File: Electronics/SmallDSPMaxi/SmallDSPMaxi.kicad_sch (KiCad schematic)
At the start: 94 parts, among them J1 Header, J10 Header, J11 Programming, J2 Header, J3 Header, J4 Header, J5 Header, J6 Header, J7 Header, J8 Header, J9 Header, Q1 NSS1C300ET4G, SW1 SW_4PDT, SW2 TS-1187A-B-A-B, SW3 CJS-1201TB, U1 ADAU1467, U2 ADM811, U3 M95M01-R, Y1 830105957509

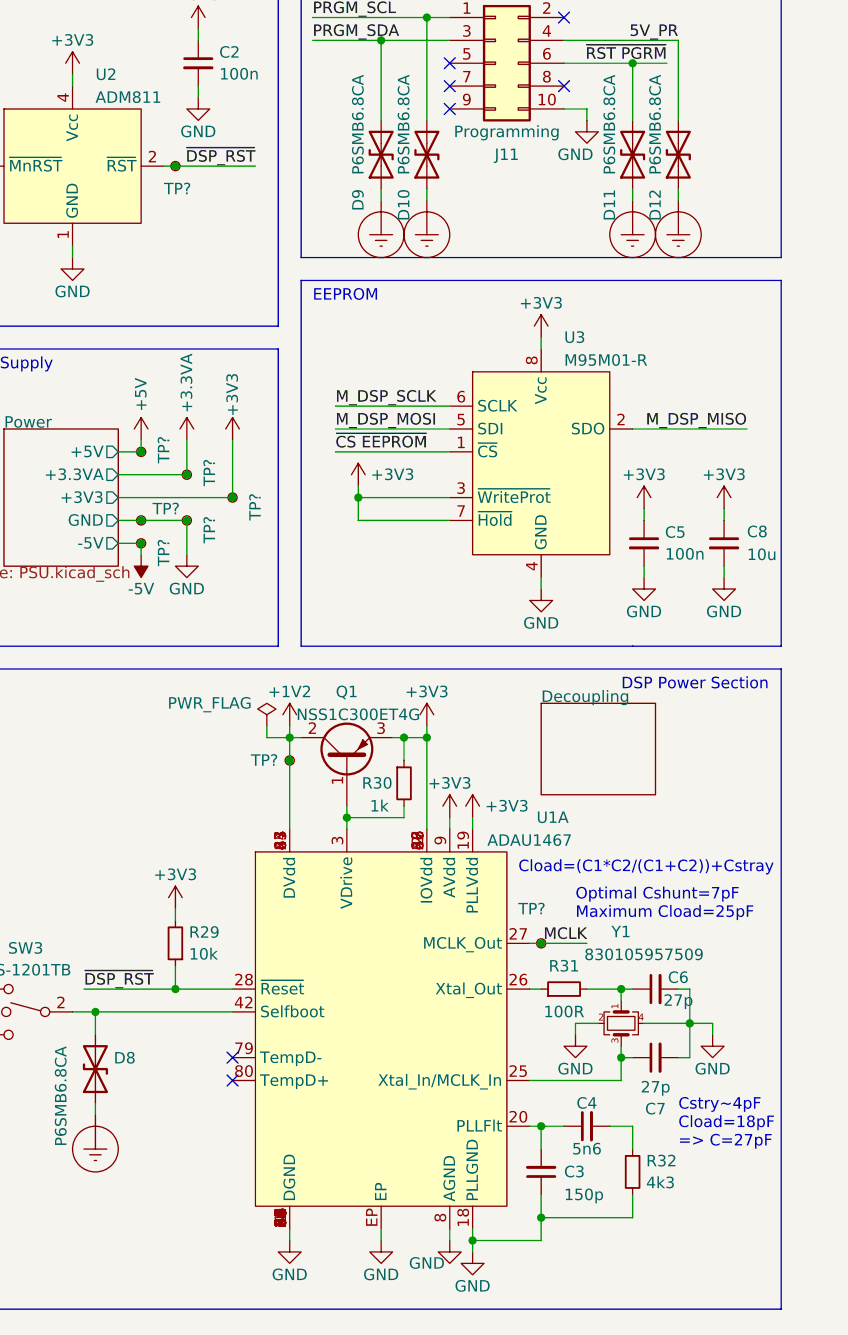
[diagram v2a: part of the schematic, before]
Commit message: Fixes schematic mistakes, like incorrect routin of clock to codecs
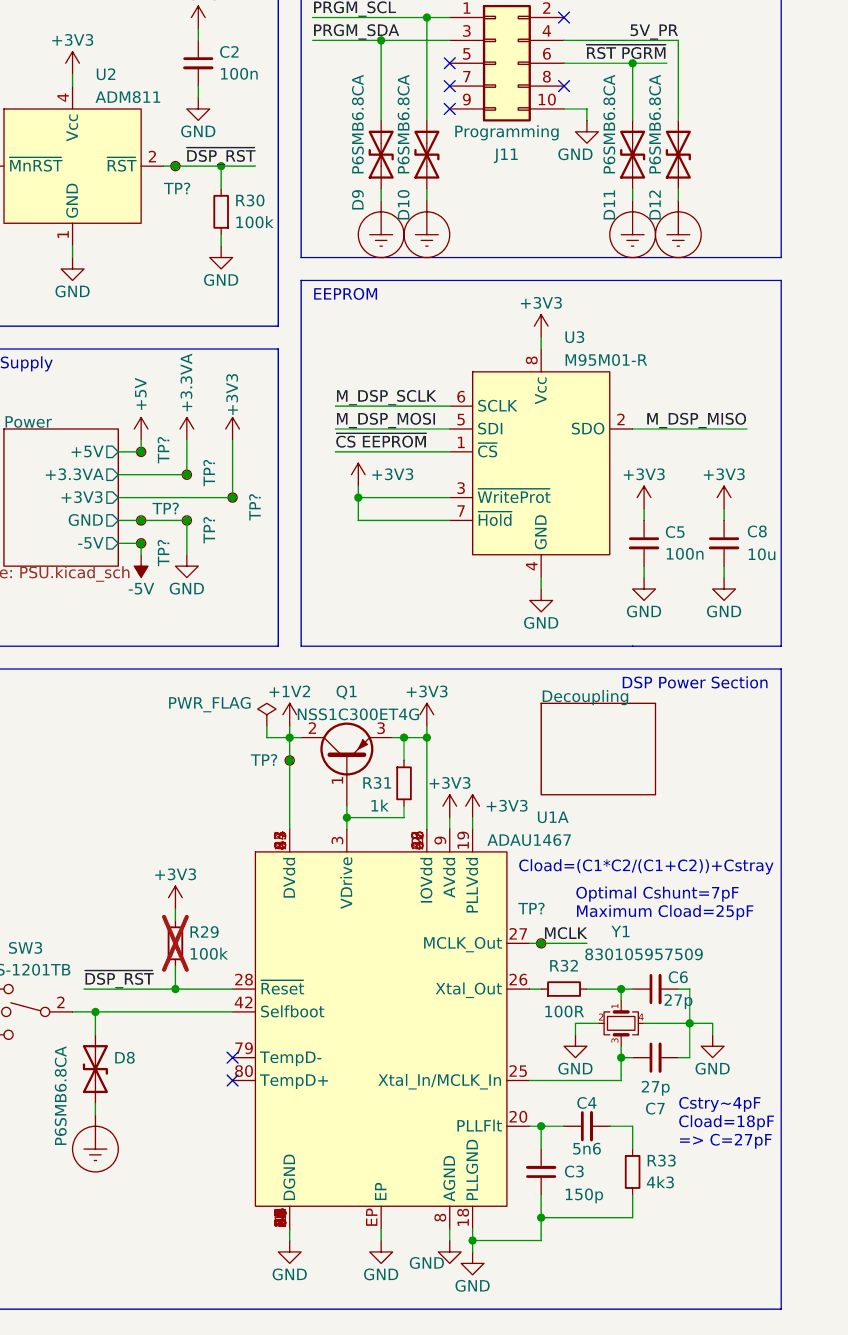
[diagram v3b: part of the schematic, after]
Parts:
- added R30: 100k, Resistor_SMD:R_0402_1005Metric, symbol Device:R_Small
- R29: value 10k -> 100k; LCSC Part # C25744 -> C25741; Part Number 0402WGF1002TCE -> 0402WGF1003TCE; now not fitted
- renumbered R30 to R31, R31 to R32, R32 to R33
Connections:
- net GND: now also R30.1
- net ~{DSP_RST}: now also R30.2

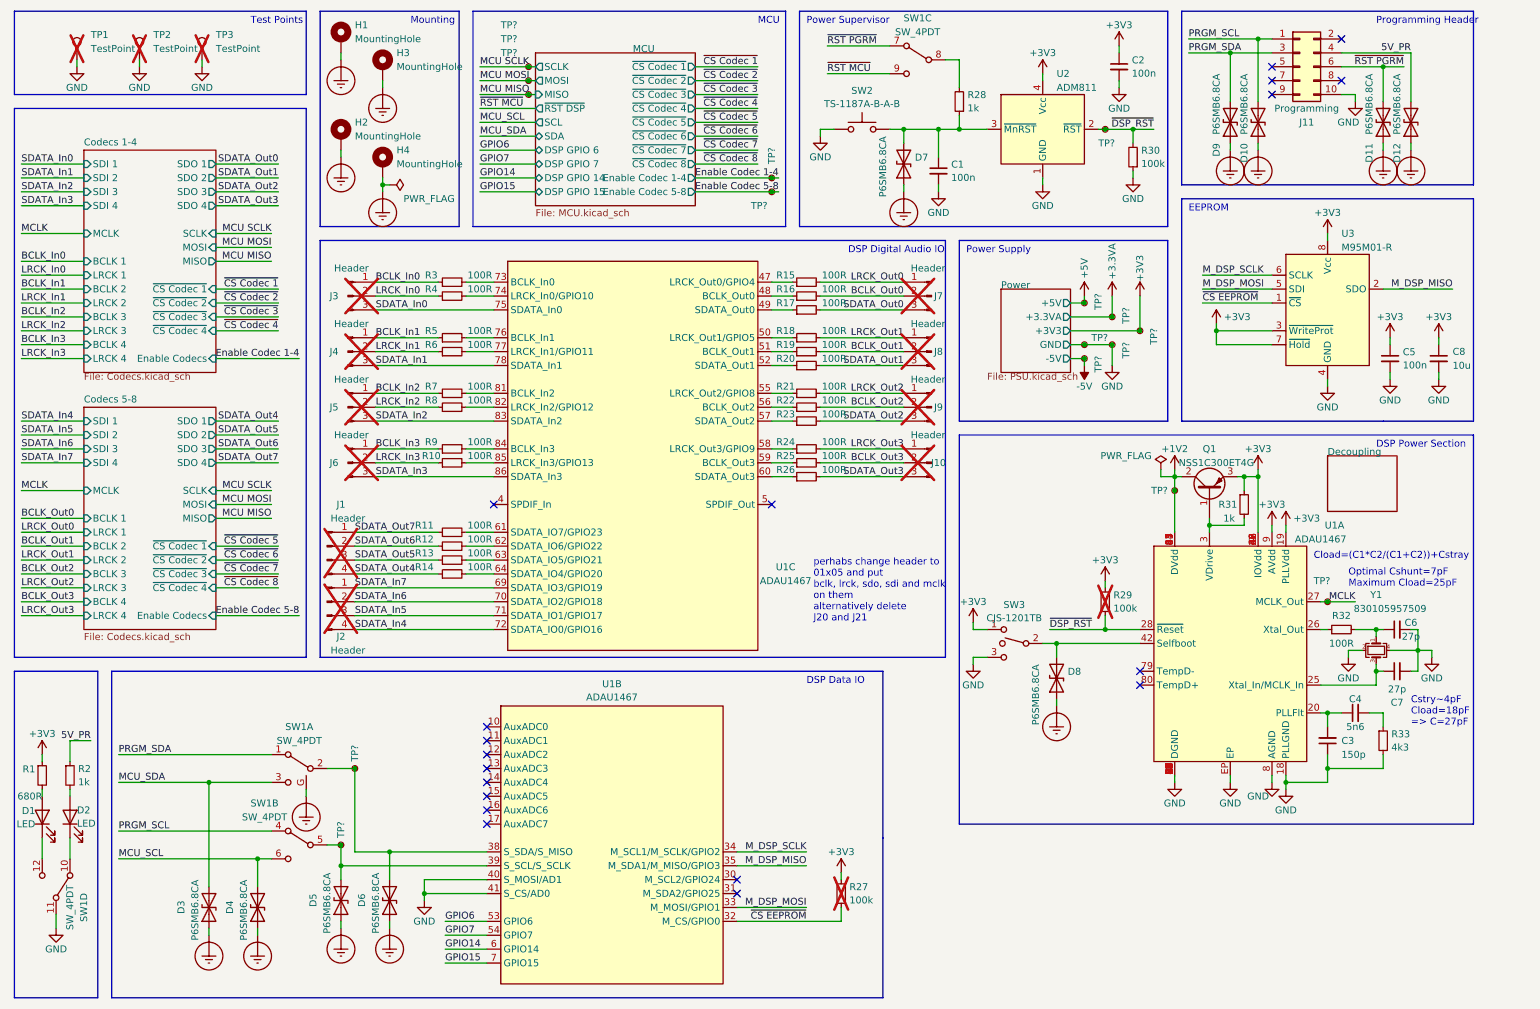
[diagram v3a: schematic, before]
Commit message: Wires DSP programming port to SPI instead of I2C
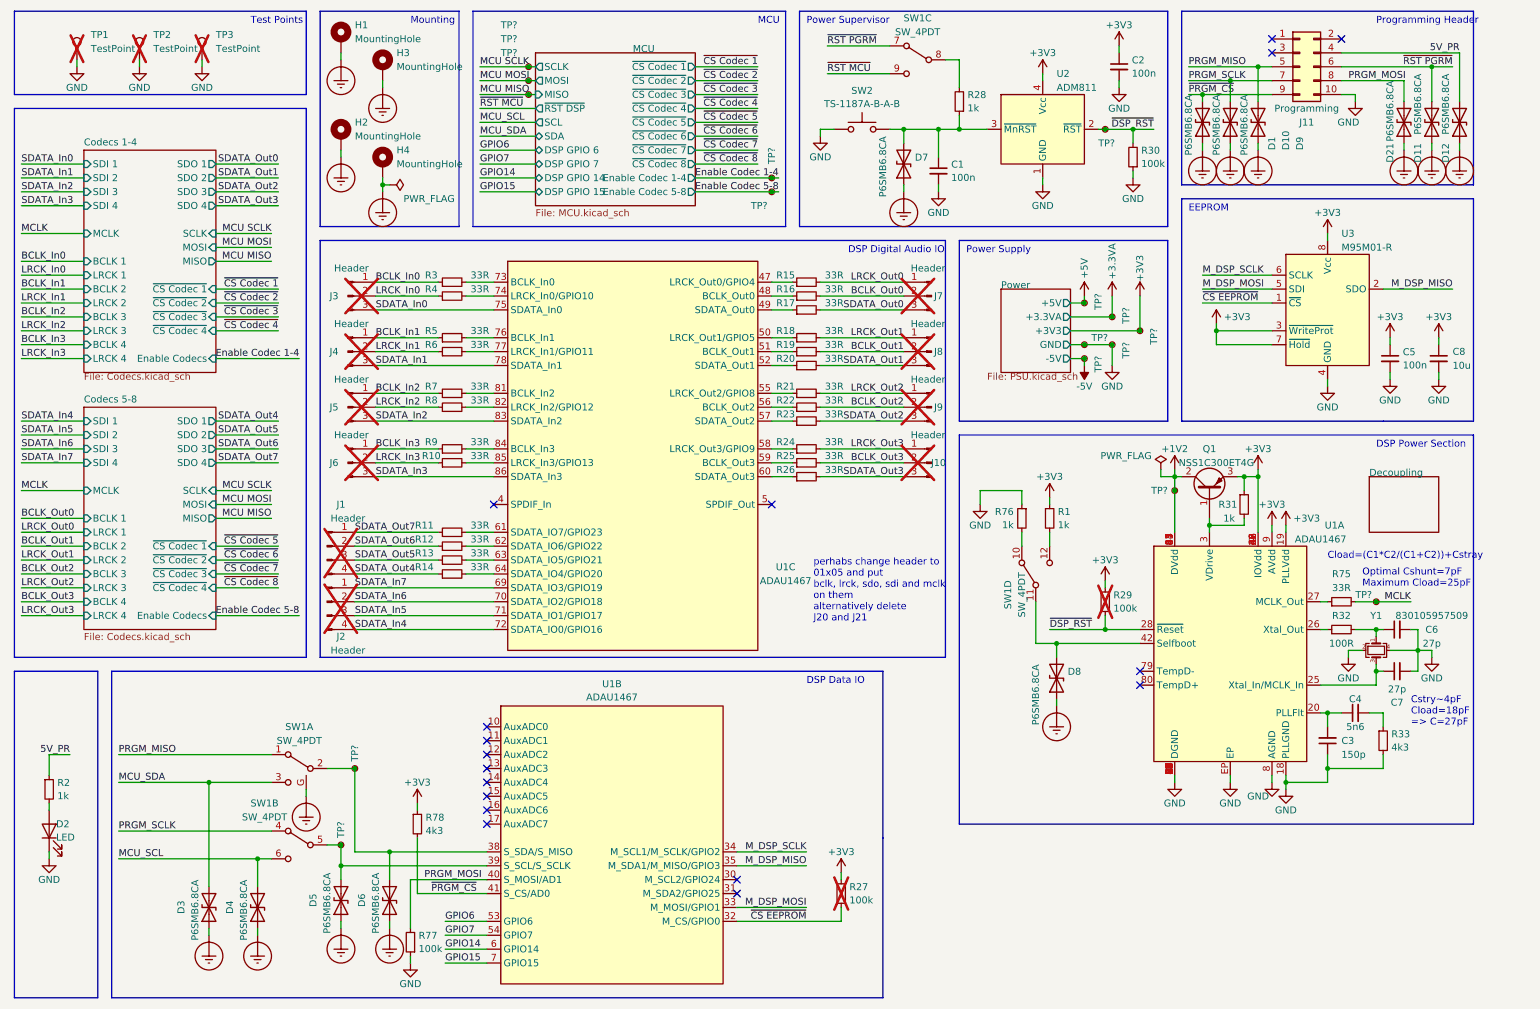
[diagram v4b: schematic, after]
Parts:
- removed D1: LED, Connector_PinHeader_1.27mm:PinHeader_1x02_P1.27mm_Vertical, symbol Device:LED
- removed SW3: CJS-1201TB, 1_Project_Footprints:CJS-1201TB, symbol Switch:SW_SPDT_MSM
- added D1, D21: P6SMB6.8CA, Diode_SMD:D_SMB, symbol Device:D_TVS
- added R75: 33R, Resistor_SMD:R_0402_1005Metric, symbol Device:R_Small
- added R76: 1k, Resistor_SMD:R_0402_1005Metric, symbol Device:R_Small
- added R77: 100k, Resistor_SMD:R_0402_1005Metric, symbol Device:R_Small
- added R78: 4k3, Resistor_SMD:R_0603_1608Metric, symbol Device:R_Small
- R1: value 680R -> 1k; LCSC Part # C25130 -> C11702; Part Number 0402WGF6800TCE -> 0402WGF1001TCE
- R10, R11, R12, R13, R14, R15, R16, R17, R18, R19, R20, R21, R22, R23, R24, R25, R26, R3, R4, R5, R6, R7, R8, R9: value 100R -> 33R; LCSC Part # C25076 -> C25105; Part Number 0402WGF1000TCE -> 0402WGF330JTCE
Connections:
- net +3V3: now also R78.1
- net Earth_Protective: now also D1.1 (A1), D21.1 (A1)
- net GND: now also D2.1 (K), R76.1, R77.1; no longer SW1.11 (B), U1.40 (S_MOSI/AD1), U1.41 (S_CS/AD0)
- net MCLK: now also R75.2; no longer U1.27 (MCLK_Out)
- net at D8.2 (A2), U1.42 (Selfboot): now also SW1.11 (B)
- net at SW1.10 (A): now also R76.2; no longer D2.1 (K)
- net at SW1.12 (C): now also R1.2
- net PRGM_MISO: now reaches J11.5 (Pin_5)
- net PRGM_MISO: now also D9.2 (A2), SW1.1 (A)
- net PRGM_SCLK: now reaches J11.7 (Pin_7)
- net PRGM_SCLK: now also D10.2 (A2), SW1.4 (A)
- net PRGM_MOSI: now reaches J11.8 (Pin_8)
- net PRGM_MOSI: now also U1.40 (S_MOSI/AD1), D21.2 (A2), R77.2
- net ~{PRGM_CS}: now reaches J11.9 (Pin_9)
- net ~{PRGM_CS}: now also U1.41 (S_CS/AD0), D1.2 (A2), R78.2
- removed net PRGM_SCL: D10.2 (A2), J11.1 (Pin_1), SW1.4 (A)
- removed net PRGM_SDA: D9.2 (A2), J11.3 (Pin_3), SW1.1 (A)
- new net: R75.1, U1.27 (MCLK_Out)
- no-connect marks 19 -> 17
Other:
- moved on the sheet: D10, D11, D12, D2, D9, R2, SW1D, TP?

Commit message: Adds clock distributer
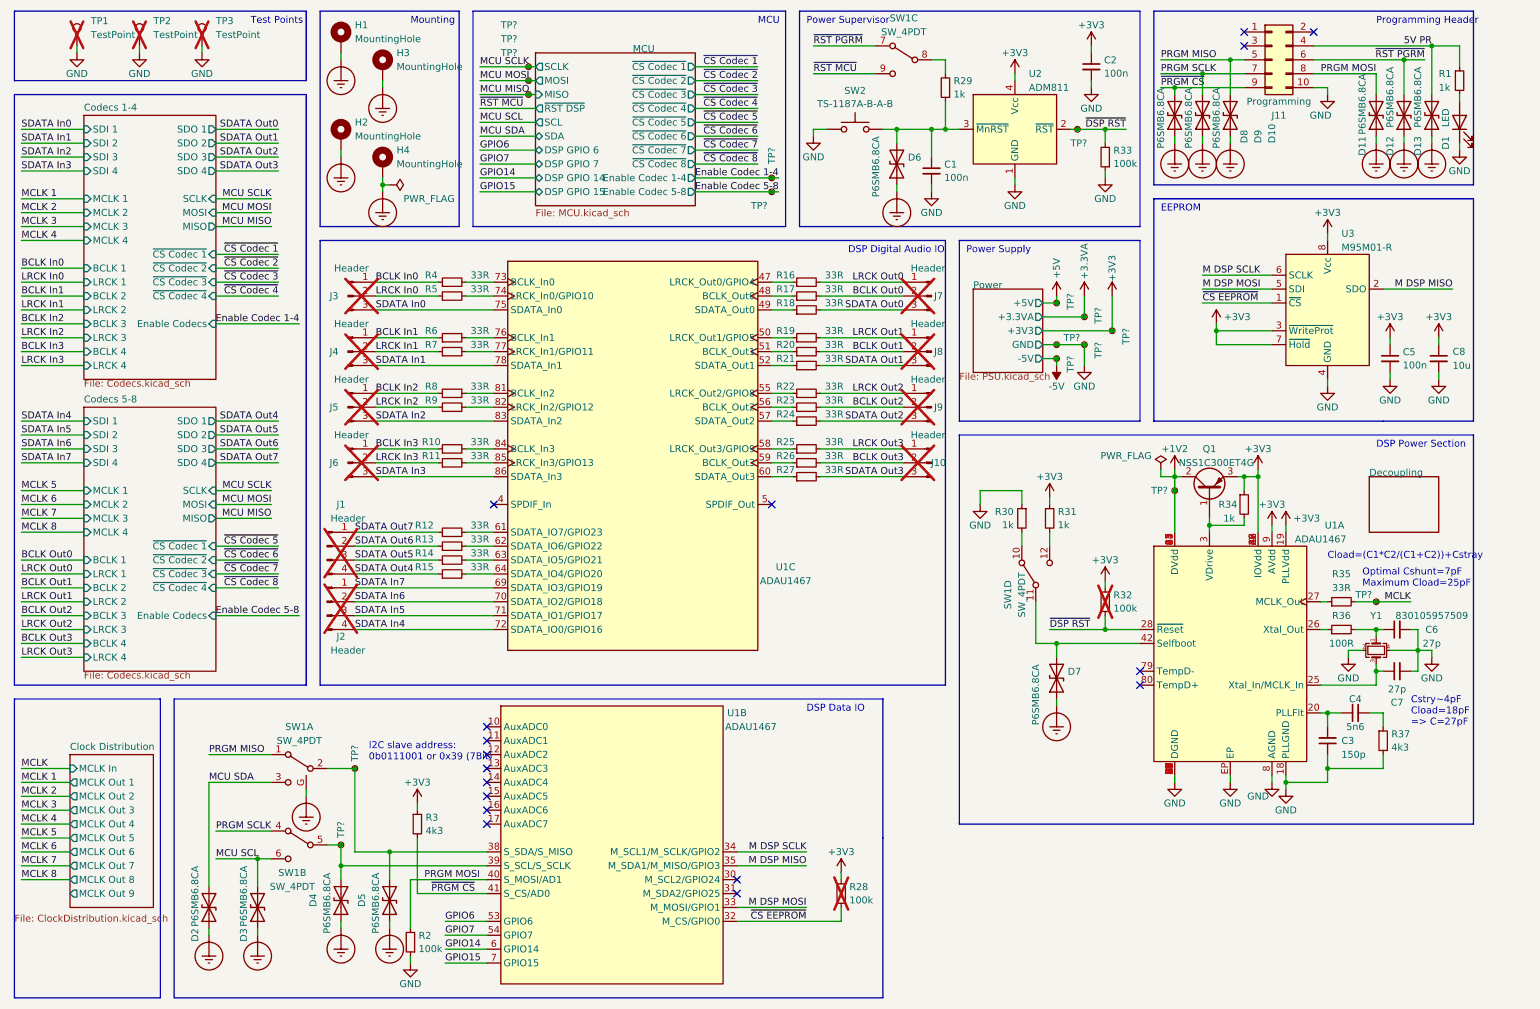
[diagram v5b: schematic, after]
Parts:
- U1: Part Number ADAU1467WBCPZ300 -> ADAU1463
- renumbered D2 to D1, D9 to D10, D21 to D11, D11 to D12, D12 to D13, D3 to D2, D4 to D3, D5 to D4, D6 to D5, D7 to D6, D8 to D7, D1 to D8, D10 to D9, R2 to R1, R9 to R10, R10 to R11, R11 to R12, R12 to R13, R13 to R14, R14 to R15, R15 to R16, R16 to R17, R17 to R18, R18 to R19, R77 to R2, R19 to R20, R20 to R21, R21 to R22, R22 to R23, R23 to R24, R24 to R25, R25 to R26, R26 to R27, R27 to R28, R28 to R29, R78 to R3, R76 to R30, R1 to R31, R29 to R32, R30 to R33, R31 to R34, R75 to R35, R32 to R36, R33 to R37, R3 to R4, R4 to R5, R5 to R6, R6 to R7, R7 to R8, R8 to R9
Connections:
- net 5V_PR renamed 5V PR
- net BCLK_In0 renamed BCLK In0
- net BCLK_In1 renamed BCLK In1
- net BCLK_In2 renamed BCLK In2
- net BCLK_In3 renamed BCLK In3
- net BCLK_Out0 renamed BCLK Out0
- net BCLK_Out1 renamed BCLK Out1
- net BCLK_Out2 renamed BCLK Out2
- net BCLK_Out3 renamed BCLK Out3
- net LRCK_In0 renamed LRCK In0
- net LRCK_In1 renamed LRCK In1
- net LRCK_In2 renamed LRCK In2
- net LRCK_In3 renamed LRCK In3
- net LRCK_Out0 renamed LRCK Out0
- net LRCK_Out1 renamed LRCK Out1
- net LRCK_Out2 renamed LRCK Out2
- net LRCK_Out3 renamed LRCK Out3
- net MCU_SCL renamed MCU SCL
- net MCU_SDA renamed MCU SDA
- net M_DSP_MISO renamed M DSP MISO
- net M_DSP_MOSI renamed M DSP MOSI
- net M_DSP_SCLK renamed M DSP SCLK
- net PRGM_MISO renamed PRGM MISO
- net PRGM_MOSI renamed PRGM MOSI
- net PRGM_SCLK renamed PRGM SCLK
- net SDATA_In0 renamed SDATA In0
- net SDATA_In1 renamed SDATA In1
- net SDATA_In2 renamed SDATA In2
- net SDATA_In3 renamed SDATA In3
- net SDATA_In4 renamed SDATA In4
- net SDATA_In5 renamed SDATA In5
- net SDATA_In6 renamed SDATA In6
- net SDATA_In7 renamed SDATA In7
- net SDATA_Out0 renamed SDATA Out0
- net SDATA_Out1 renamed SDATA Out1
- net SDATA_Out2 renamed SDATA Out2
- net SDATA_Out3 renamed SDATA Out3
- net SDATA_Out4 renamed SDATA Out4
- net SDATA_Out5 renamed SDATA Out5
- net SDATA_Out6 renamed SDATA Out6
- net SDATA_Out7 renamed SDATA Out7
- net ~{DSP_RST} renamed ~{DSP RST}
- net ~{PRGM_CS} renamed ~{PRGM CS}
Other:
- added sheet Clock Distribution (ClockDistribution.kicad_sch)
- sheet Codecs 1-4 ports: added MCLK 1, MCLK 2, MCLK 3, MCLK 4; removed MCLK
- sheet Codecs 5-8 ports: added MCLK 1, MCLK 2, MCLK 3, MCLK 4; removed MCLK
- note added: "I2C slave address: 0b0111001 or 0x39 (7Bit)"
- note removed: "perhabs change header to 01x05 and put bclk, lrck, sdo, sdi and mclk on them alternatively delete J20 and J21"
- title: SmallDSP -> SmallDSP Maxi
- moved on the sheet: C1, C2, D1, D10, D11, D12, D13, D6, D8, D9, J11, R1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
